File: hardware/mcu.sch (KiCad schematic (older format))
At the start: 48 parts, among them P2 CONN_02X05_JTAG, P5 CONN_01X08_DEBUG, P6 CONN_01X03_UART, P7 CONN_01X03_CAN, P8 CONN_01X05_ENCODER, SW2 SW_PUSH, U11 TM4C1294KCPDT, U18 SN65HVD231D, U21 74LVCH2T45, Y1 NX5032GA

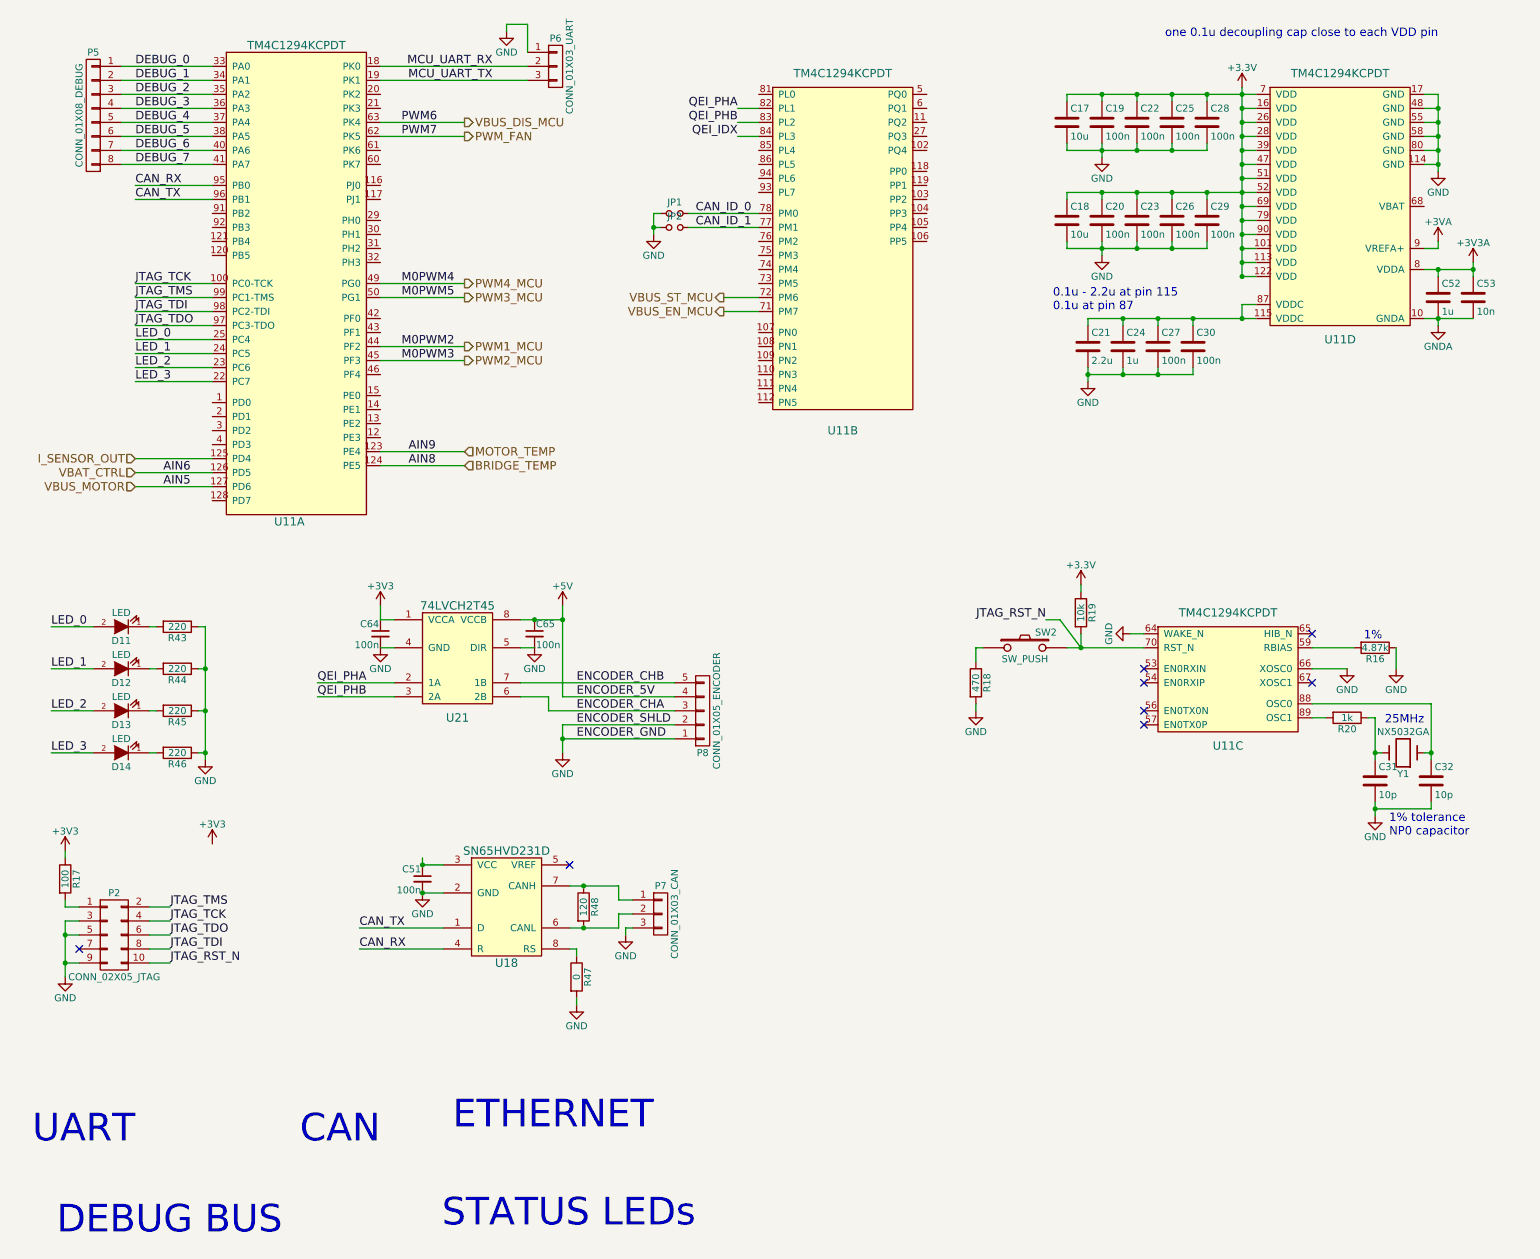
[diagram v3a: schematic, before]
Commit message: H-bridge decoupling, footprints, mechanical
- Finished H-bridge decoupling study and chose H-bridge caps
- Changed LT3471 inductors to those found in reference design,
  made footprints for them
- Swapped Si86xx isolator for Si80xx (smaller package)
- Updated heatsink footprint with correct screw sizes
- Created mechanical hole footprints (M3, M4 screws)
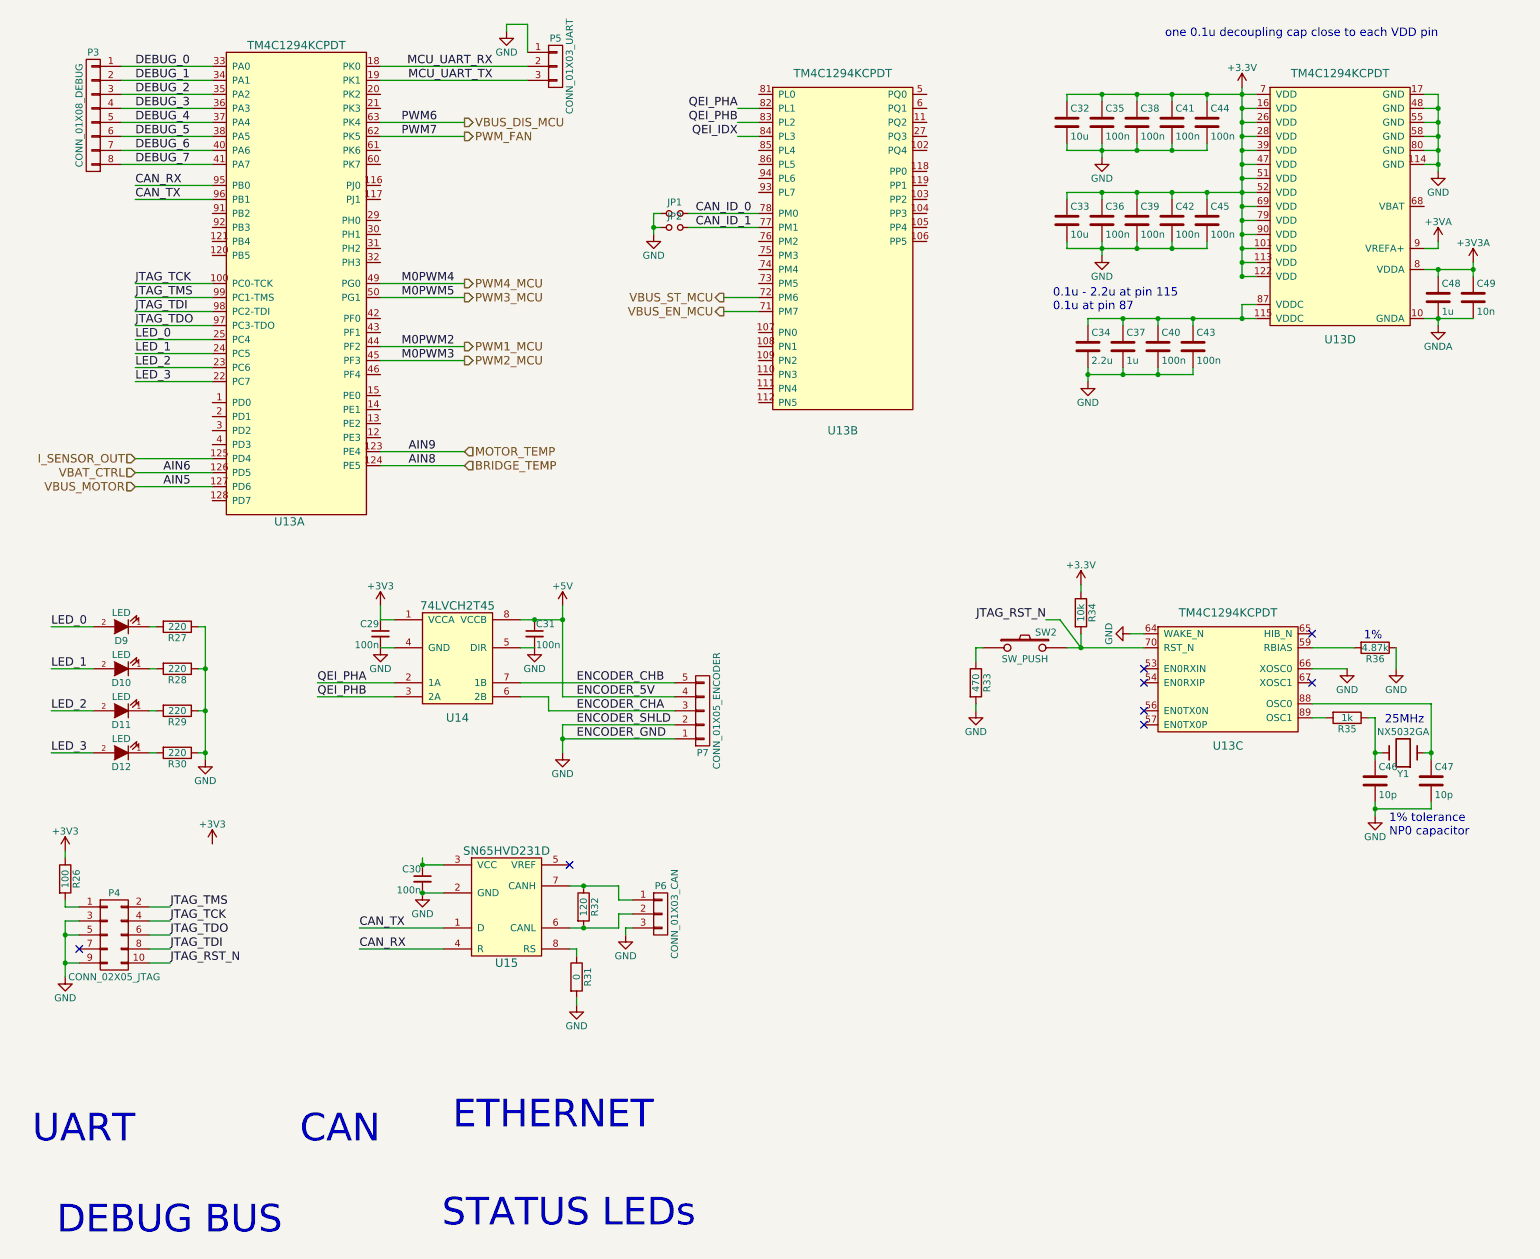
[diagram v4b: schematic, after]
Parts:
- renumbered C64 to C29, C51 to C30, C65 to C31, C17 to C32, C18 to C33, C21 to C34, C19 to C35, C20 to C36, C24 to C37, C22 to C38, C23 to C39, C27 to C40, C25 to C41, C26 to C42, C30 to C43, C28 to C44, C29 to C45, C31 to C46, C32 to C47, C52 to C48, C53 to C49, D12 to D10, D13 to D11, D14 to D12, D11 to D9, P5 to P3, P2 to P4, P6 to P5, P7 to P6, P8 to P7, R17 to R26, R43 to R27, R44 to R28, R45 to R29, R46 to R30, R47 to R31, R48 to R32, R18 to R33, R19 to R34, R20 to R35, R16 to R36, U11 to U13, U21 to U14, U18 to U15

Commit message: Bulk cap layout, diodes, lugs, leds, trimpots
- Moved H-bridge bulk capacitors to horizontal layout
- Changed H-bridge and fan diodes to 100V schottky
- Made 4AWG lug mount footprint, added lugs to BOM
- Tweaked LED resistor values, added LEDs to BOM
- Made trimpot footprint, added trimpots to BOM
- Added snubber to ferrite bead circuit; also added FB to BOM
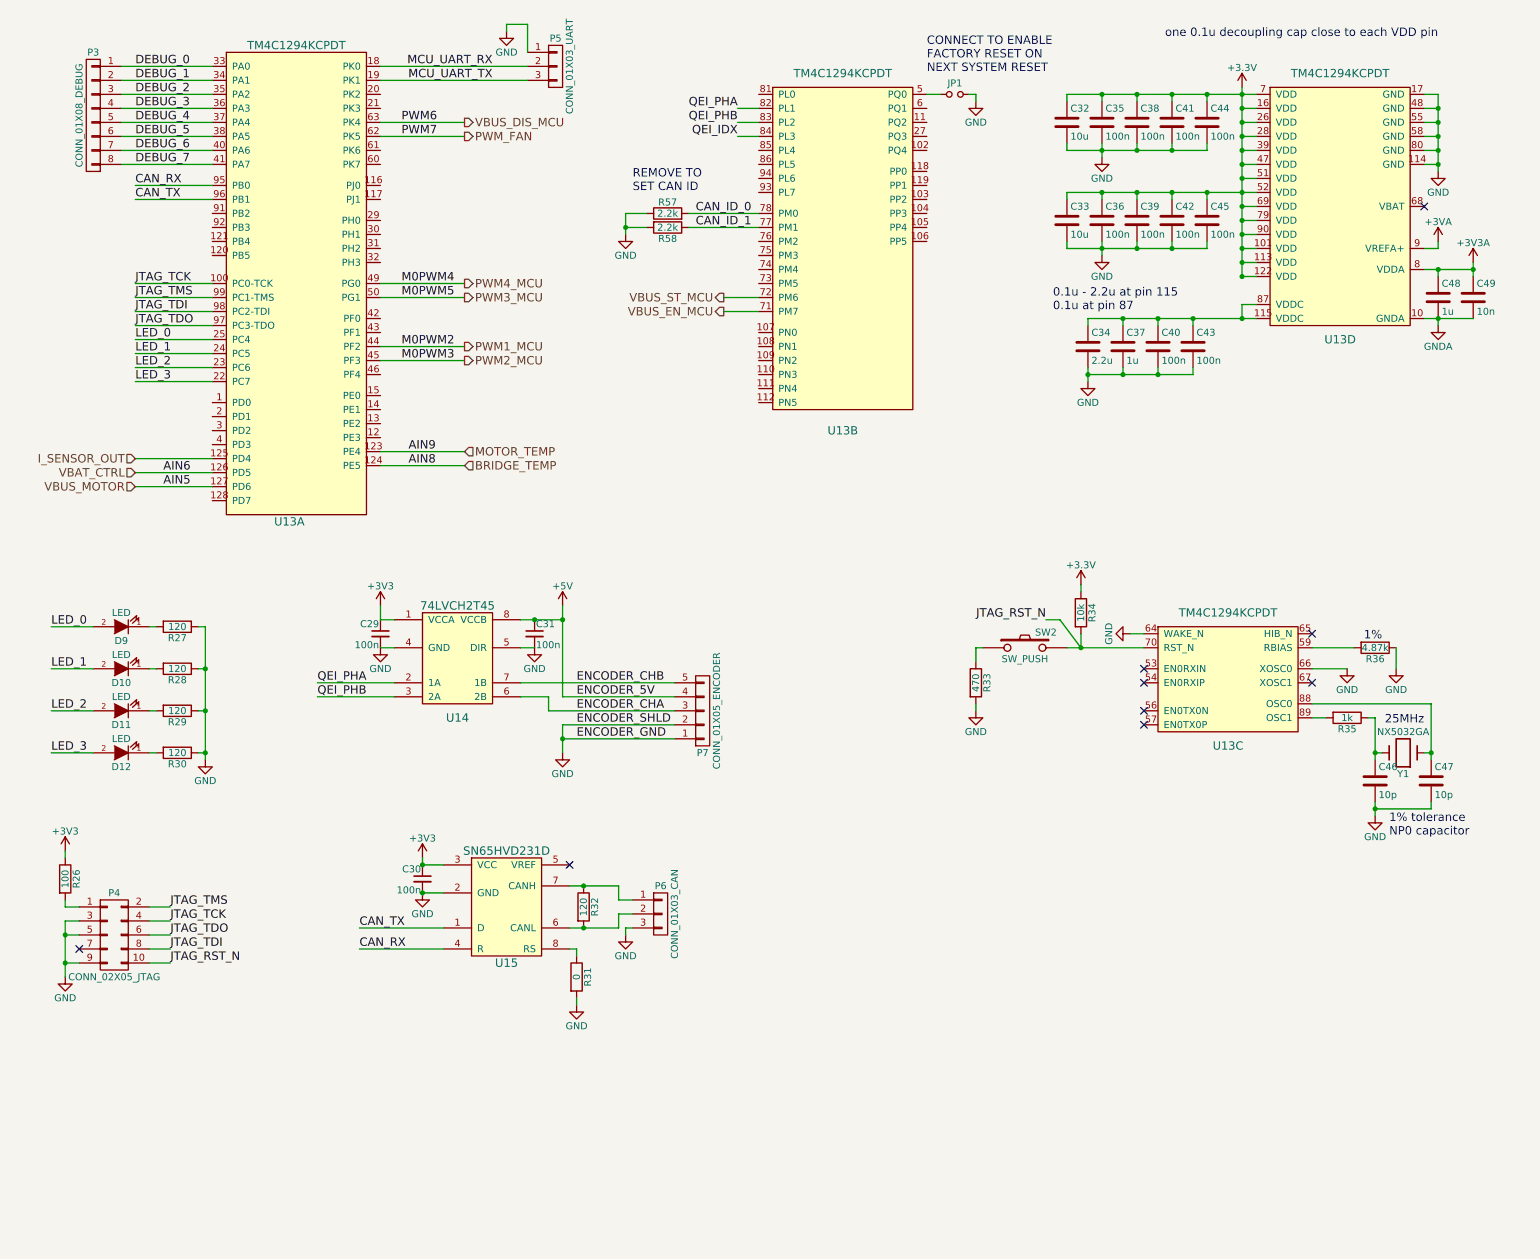
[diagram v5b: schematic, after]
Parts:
- removed JP2: Jumper_NO_Small, Pin_Headers:Pin_Header_Straight_1x02, symbol Jumper_NO_Small
- added R57, R58: 2.2k, Resistors_SMD:R_0603, symbol R
- D10, D11, D12, D9: footprint (none) -> LEDs:LED_0603
- P5: footprint 2kwMotorController:TERM_3P_2-5_1990012 -> Pin_Headers:Pin_Header_Straight_1x03
- R27, R28, R29, R30: value 220 -> 120
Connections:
- net +3V3: now also C30.1, U15.3 (VCC)
- net CAN_ID_0: now also R57.2; no longer JP1.2
- net CAN_ID_1: now also R58.1
- net GND: now also JP1.2, R57.1, R58.2; no longer JP1.1
- net at U13.5 (PQ0): now also JP1.1
- no-connect marks 8 -> 9
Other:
- note added: "CONNECT TO ENABLE\nFACTORY RESET ON\nNEXT SYSTEM RESET"
- note added: "REMOVE TO \nSET CAN ID"
- note removed: "CAN"
- note removed: "DEBUG BUS"
- note removed: "ETHERNET"
- note removed: "STATUS LEDs"
- note removed: "UART"
